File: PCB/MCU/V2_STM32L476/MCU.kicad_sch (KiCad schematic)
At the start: 71 parts, among them IC2 LTC4311CSC6#TRPBF, J1 Conn_02x06_Odd_Even, J2 Conn_02x06_Odd_Even, J3 Conn_ARM_SWD_TagConnect_TC203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, J4 Conn_01x04_Pin, J5 RESET, J6 Conn_01x04_Pin, J7 USB_B_Micro, Q1 PJE8408_R1_00001, Q2 PJE8408_R1_00001, U1 MB85RS2MTAPNF-G-BDERE1, U3 MAX6372, U4 ADP160AUJZ-3.3-R7, U5 ICM-20948, U6 ADP160AUJZ-1.8, U7 STM32L476RGT6, U8 AP2112K-3.3, U9 HexSense_MCU_dev_board, Y2 32KHz, Y3 ECS-160-12-33-AGN-TR3

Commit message: mac:working on the stm32l476 mcu board
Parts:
- removed C25, C27: 0.1uF, Capacitor_SMD:C_0402_1005Metric_Pad0.74x0.62mm_HandSolder, symbol Device:C_Small
- removed C28: 10uF, PCM_JLCPCB:C_1206, symbol PCM_JLCPCB-Capacitors:1206,10uF
- removed C7: 0.01uF, Capacitor_SMD:C_0402_1005Metric_Pad0.74x0.62mm_HandSolder, symbol Device:C_Small
- removed D3: Blue, LED_SMD:LED_0402_1005Metric_Pad0.77x0.64mm_HandSolder, symbol Device:LED_Filled
- removed D4: Red, LED_SMD:LED_0402_1005Metric_Pad0.77x0.64mm_HandSolder, symbol Device:LED_Filled
- removed D5: MBR1020VL, Diode_SMD:D_SOD-123F, symbol Diode:MBR1020VL
- removed J3: Conn_ARM_SWD_TagConnect_TC2030-NL, Connector:Tag-Connect_TC2030-IDC-NL_2x03_P1.27mm_Vertical, symbol Connector:Conn_ARM_SWD_TagConnect_TC2030-NL
- removed J4: Conn_01x04_Pin, Connector_PinHeader_2.54mm:PinHeader_1x04_P2.54mm_Vertical, symbol Connector:Conn_01x04_Pin
- removed J7: USB_B_Micro, Connector_USB:USB_Micro-B_Molex_47346-0001, symbol Connector:USB_B_Micro
- removed R20: 10K, Resistor_SMD:R_0603_1608Metric_Pad0.98x0.95mm_HandSolder, symbol Device:R_Small
- removed R23: 10kΩ, Resistor_SMD:R_0402_1005Metric_Pad0.72x0.64mm_HandSolder, symbol PCM_JLCPCB-Resistors:0603,1kΩ
- removed R24: 4.7kΩ, Resistor_SMD:R_0402_1005Metric_Pad0.72x0.64mm_HandSolder, symbol PCM_JLCPCB-Resistors:0603,1kΩ
- removed R26: 10kΩ, PCM_JLCPCB:R_0603, symbol PCM_JLCPCB-Resistors:0603,1kΩ
- removed R27: 10K, Resistor_SMD:R_0402_1005Metric_Pad0.72x0.64mm_HandSolder, symbol Device:R_Small
- removed R5, R6: 27, Resistor_SMD:R_0402_1005Metric_Pad0.72x0.64mm_HandSolder, symbol Device:R_Small
- removed S1: SKQGAKE010, SamacSys_Parts:SKQGAKE010, symbol SamacSys_Parts:SKQGAKE010
- removed TP1: BAT_TP, TestPoint:TestPoint_Pad_1.0x1.0mm, symbol Connector:TestPoint_Alt
- removed TP4, TP5, TP6, TP7: TestPoint, TestPoint:TestPoint_Pad_D1.0mm, symbol Connector:TestPoint
- removed U8: AP2112K-3.3, Package_TO_SOT_SMD:SOT-23-5, symbol Regulator_Linear:AP2112K-3.3
- removed U9: HexSense_MCU_dev_board, Mylib:HexSense_MCU_dev_board, symbol Mylib:HexSense_DEV_brd_MCU_brd
- added R1, R2: 4.7kΩ, PCM_JLCPCB:R_0402, symbol PCM_JLCPCB-Resistors:0402,4.7kΩ
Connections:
- net +5V is gone; now on net +3.3V: J6.1 (Pin_1)
- net SCL is gone; now on net I2C2_SCL: IC2.4 (BUS2), J1.12 (Pin_12), Q2.3
- net SDA is gone; now on net I2C2_SDA: IC2.6 (BUS1), J1.11 (Pin_11), Q1.3
- net VCC is gone; now on net +3.3V: C1.1, C10.1, C3.1, C9.2, IC2.1 (VCC), R12.2, R13.2, U1.8 (VDD), U3.4 (SET0), U3.5 (SET1), U3.6 (SET2), U3.8 (VCC), U4.5 (VOUT)
- net ~{RESET} is gone; now on net NRST: R9.2
- net +3.3V: now also R1.1, R2.1
- net I2C2_SCL: now also R1.2
- net I2C2_SDA: now also R2.2
- net MISO: no longer J2.9 (Pin_9)
- net MOSI: no longer J2.3 (Pin_3)
- net PA3: now also R22.2
- net PC4: no longer R22.2
- net SCK: no longer J2.5 (Pin_5)
- net SPI1_MISO: now also J2.9 (Pin_9)
- net SPI1_MOSI: now also J2.3 (Pin_3)
- net SPI1_SCK: now also J2.5 (Pin_5)
- net SWDCLK: now also J6.2 (Pin_2)
- net SWDIO: now also J6.3 (Pin_3)
- no-connect marks 19 -> 13
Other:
- note added: "SWD"
- note removed: "USB"
- moved on the sheet: C1, C10, C11, C14, C16, C17, C18, C19, C20, C21, C22, C23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

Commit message: mac: finishing the L476 mcu board
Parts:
- added R4: 10K, Resistor_SMD:R_0402_1005Metric_Pad0.72x0.64mm_HandSolder, symbol Device:R_Small
- R9: value 330 -> 0; footprint Resistor_SMD:R_0402_1005Metric_Pad0.72x0.64mm_HandSolder -> Resistor_SMD:R_0201_0603Metric
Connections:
- net 1V8_EN is gone; now on net PA12: U6.3 (EN)
- net A2 is gone; now on net SPI3_MISO: J1.6 (Pin_6)
- net A3 is gone; now on net PA9: J1.4 (Pin_4)
- net A4 is gone; now on net PC4: J2.8 (Pin_8)
- net A5 is gone; now on net SPI3_MOSI: J1.3 (Pin_3)
- net D1 is gone; now on net PB0: J2.4 (Pin_4)
- net D10 is gone; now on net PB1: J2.2 (Pin_2)
- net D12 is gone; now on net PB2: J2.1 (Pin_1)
- net D3 is gone; now on net PC5: J2.6 (Pin_6)
- net D8 is gone; now on net PA8: J1.2 (Pin_2)
- net RXD is gone; now on net SPI3_SCK: J1.7 (Pin_7)
- net TXD is gone; now on net SPI3_CS: J1.9 (Pin_9)
- net WDI is gone; now on net PB9: U3.1 (WDI)
- net D2: no longer J2.7 (Pin_7)
- net D4: no longer J2.11 (Pin_11)
- net GND: now also R4.1
- net PA12: now also R4.2
- net PA2: now also J2.11 (Pin_11)
- net SPI1_CS: now also J2.7 (Pin_7)
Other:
- moved on the sheet: C14, J6, TP2, TP3, U6

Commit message: mac: finishing the L476 mcu board
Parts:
- added R5, R6: 10K, Resistor_SMD:R_0402_1005Metric_Pad0.72x0.64mm_HandSolder, symbol Device:R_Small
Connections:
- net GND: now also R6.1
- net PA0: now also R5.1, R6.2
- net VBAT: now also R5.2

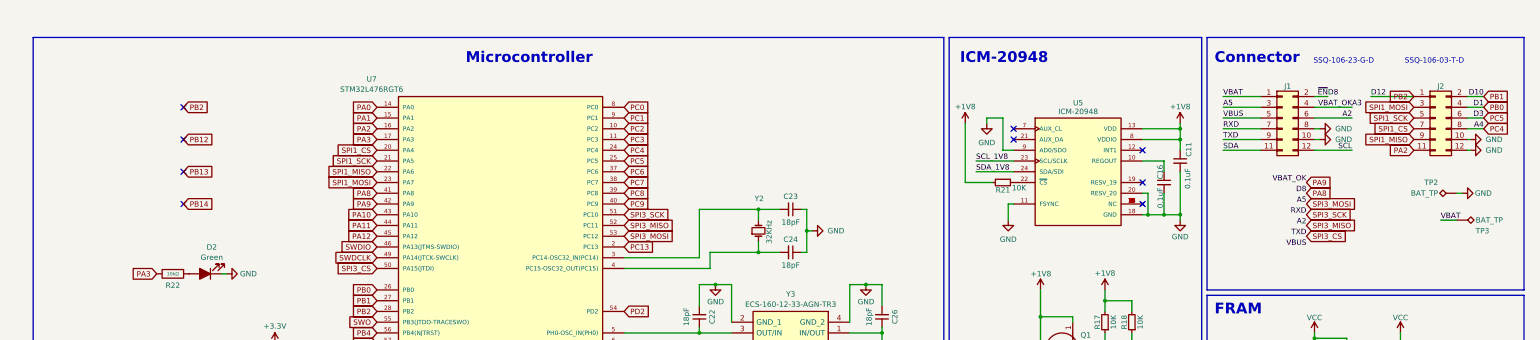
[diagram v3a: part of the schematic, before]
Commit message: pc:finished L476 MCU board
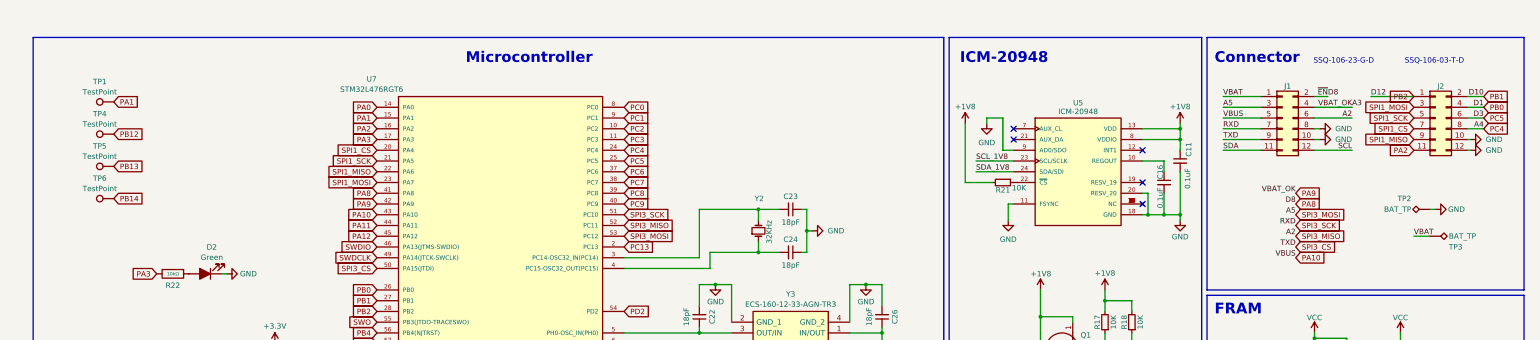
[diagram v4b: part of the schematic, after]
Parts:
- added TP1, TP4, TP5, TP6: TestPoint, TestPoint:TestPoint_Pad_D1.0mm, symbol Connector:TestPoint
- Y3: footprint SamacSys_Parts:ECS1601233AGNTR3 -> Mylib:XTAL_ECS-160-12-33-AGN-TR3
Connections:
- net VBUS is gone; now on net PA10: J1.5 (Pin_5)
- net PA1: now also TP1.1
- net PB12: now also TP4.1
- net PB13: now also TP5.1
- net PB14: now also TP6.1
- no-connect marks 13 -> 9
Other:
- moved on the sheet: TP2, TP3

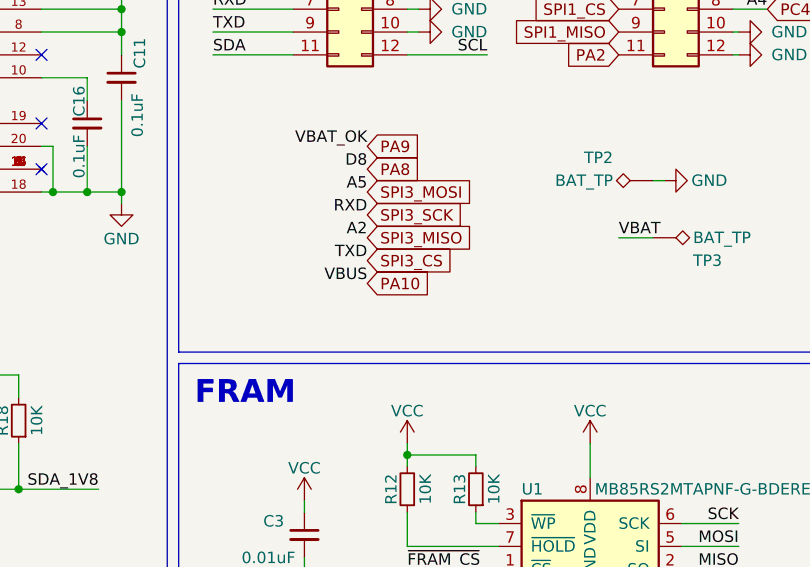
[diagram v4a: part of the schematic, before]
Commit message: pc:finished L476 MCU board
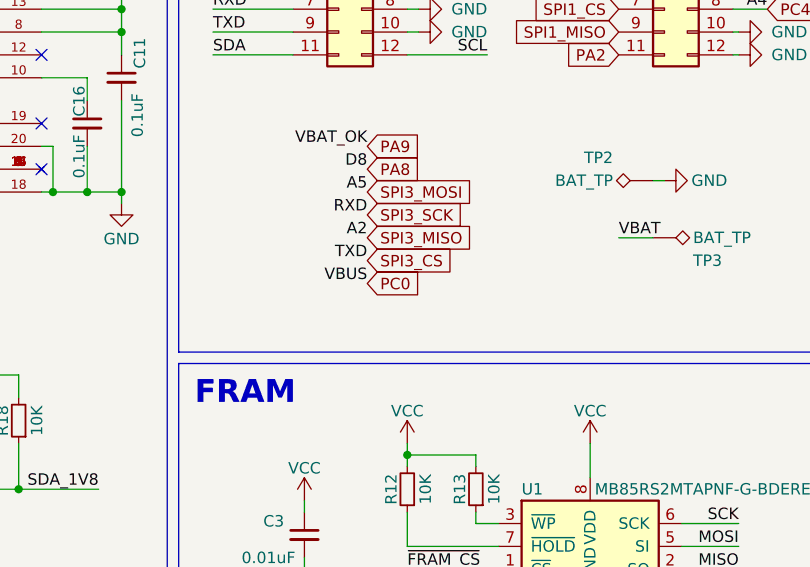
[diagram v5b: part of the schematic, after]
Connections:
- net PA10: no longer J1.5 (Pin_5)
- net PC0: now also J1.5 (Pin_5)
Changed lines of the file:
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@@
 		)
 	)
-	(global_label "PA10"
+	(global_label "PC0"
 		(shape input)
 		(at 312.42 66.04 0)
@@
 		)
 		(property "Intersheetrefs" "${INTERSHEET_REFS}"
-			(at 320.1828 66.04 0)
+			(at 319.1547 66.04 0)
 			(effects
 				(font

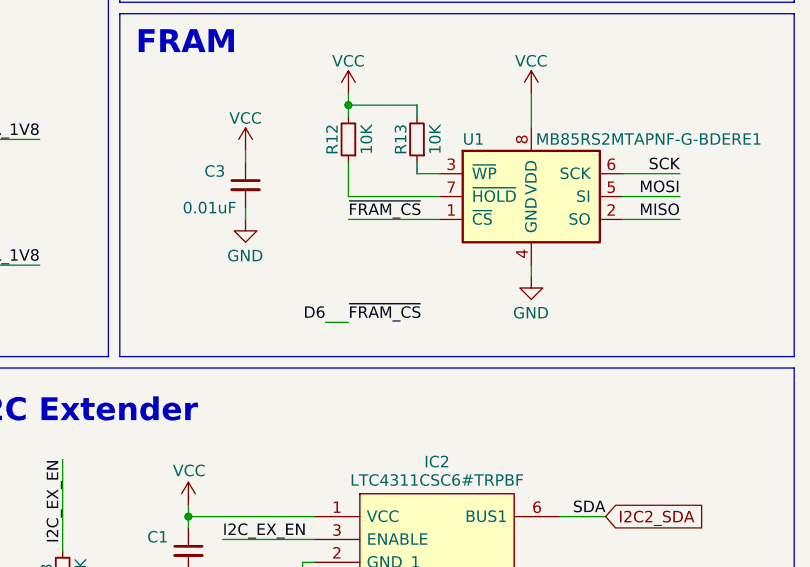
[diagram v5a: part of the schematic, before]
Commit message: mac:working on esp32s3 mcu brd, forgot the strapping pins.
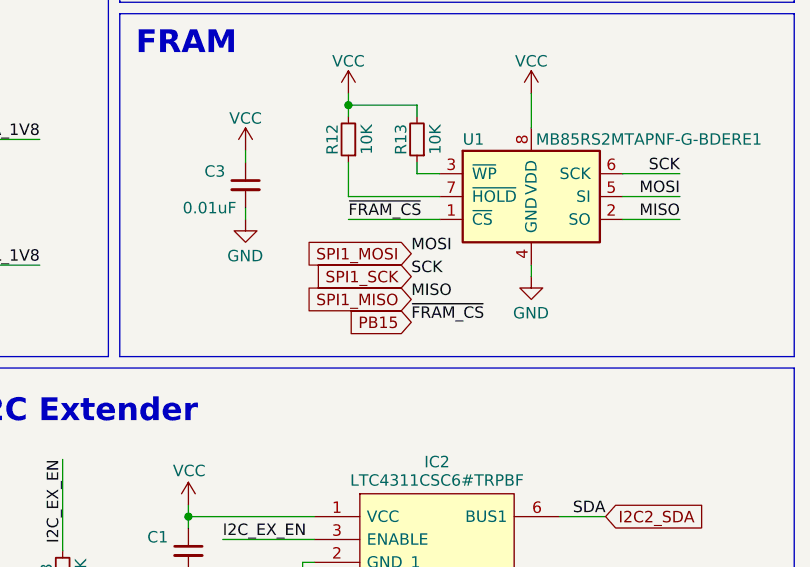
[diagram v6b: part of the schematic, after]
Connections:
- net MISO is gone; now on net SPI1_MISO: U1.2 (SO)
- net MOSI is gone; now on net SPI1_MOSI: U1.5 (SI)
- net SCK is gone; now on net SPI1_SCK: U1.6 (SCK)
- net D6: no longer U1.1 (~{CS})
- net PB15: now also U1.1 (~{CS})
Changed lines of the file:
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@@
-	(wire
-		(pts
-			(xy 314.325 109.22) (xy 316.865 109.22)
-		)
-		(stroke
-			(width 0)
-			(type default)
-		)
-	)
 	(wire
 		(pts
@@
 		)
 	)
+	(label "MOSI"
+		(at 323.85 101.6 0)
+		(effects
+			(font
+				(size 1.27 1.27)
+			)
+			(justify left bottom)
+		)
+	)
 	(label "D0"
 		(at 20.32 -49.53 0)
@@
 		)
 	)
-	(label "~{FRAM_CS}"
-		(at 316.865 109.22 0)
-		(effects
-			(font
-				(size 1.27 1.27)
-			)
-			(justify left bottom)
-		)
-	)
 	(label "A2"
 		(at 54.61 -52.07 180)
@@
 		)
 	)
+	(label "SCK"
+		(at 323.85 104.14 0)
+		(effects
+			(font
+				(size 1.27 1.27)
+			)
+			(justify left bottom)
+		)
+	)
 	(label "VBAT_OK"
 		(at 325.755 30.48 180)
@@
 		)
 	)
+	(label "MISO"
+		(at 323.85 106.68 0)
+		(effects
+			(font
+				(size 1.27 1.27)
+			)
+			(justify left bottom)
+		)
+	)
 	(label "WDI"
 		(at 140.97 148.59 0)
@@
 		)
 	)
+	(label "~{FRAM_CS}"
+		(at 323.85 109.22 0)
+		(effects
+			(font
+				(size 1.27 1.27)
+			)
+			(justify left bottom)
+		)
+	)
 	(label "RXD"
 		(at 54.61 -19.05 180)
@@
 		)
 	)
-	(label "D6"
-		(at 314.325 109.22 180)
-		(effects
-			(font
-				(size 1.27 1.27)
-			)
-			(justify right bottom)
-		)
-	)
 	(label "I2C_EX_EN"
 		(at 325.12 146.05 0)
@@
 		)
 	)
+	(global_label "SPI1_MOSI"
+		(shape input)
+		(at 323.85 101.6 180)
+		(fields_autoplaced yes)
+		(effects
+			(font
+				(size 1.27 1.27)
+			)
+			(justify right)
+		)
+		(property "Intersheetrefs" "${INTERSHEET_REFS}"
+			(at 311.0072 101.6 0)
+			(effects
+				(font
+					(size 1.27 1.27)
+				)
+				(justify right)
+				(hide yes)
+			)
+		)
+	)
 	(global_label "PC13"
 		(shape input)
@@
 		)
 	)
+	(global_label "SPI1_SCK"
+		(shape input)
+		(at 323.85 104.14 180)
+		(fields_autoplaced yes)
+		(effects
+			(font
+				(size 1.27 1.27)
+			)
+			(justify right)
+		)
+		(property "Intersheetrefs" "${INTERSHEET_REFS}"
+			(at 311.8539 104.14 0)
+			(effects
+				(font
+					(size 1.27 1.27)
+				)
+				(justify right)
+				(hide yes)
+			)
+		)
+	)
 	(global_label "PD2"
 		(shape input)
@@
 		)
 	)
+	(global_label "PB15"
+		(shape input)
+		(at 323.85 109.22 180)
+		(fields_autoplaced yes)
+		(effects
+			(font
+				(size 1.27 1.27)
+			)
+			(justify right)
+		)
+		(property "Intersheetrefs" "${INTERSHEET_REFS}"
+			(at 315.9058 109.22 0)
+			(effects
+				(font
+					(size 1.27 1.27)
+				)
+				(justify right)
+				(hide yes)
+			)
+		)
+	)
 	(global_label "PC0"
 		(shape input)
@@
 			(effects
 				(font
+					(size 1.27 1.27)
+				)
+				(justify right)
+				(hide yes)
+			)
+		)
+	)
+	(global_label "SPI1_MISO"
+		(shape input)
+		(at 323.85 106.68 180)
+		(fields_autoplaced yes)
+		(effects
+			(font
+				(size 1.27 1.27)
+			)
+			(justify right)
+		)
+		(property "Intersheetrefs" "${INTERSHEET_REFS}"
+			(at 311.0072 106.68 0)
+			(effects
+				(font
